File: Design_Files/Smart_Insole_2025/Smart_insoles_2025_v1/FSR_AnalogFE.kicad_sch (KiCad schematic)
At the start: 33 parts, among them J1 Conn_01x20, U8 MCP6004-I_ST, U9 MCP6004-I_ST

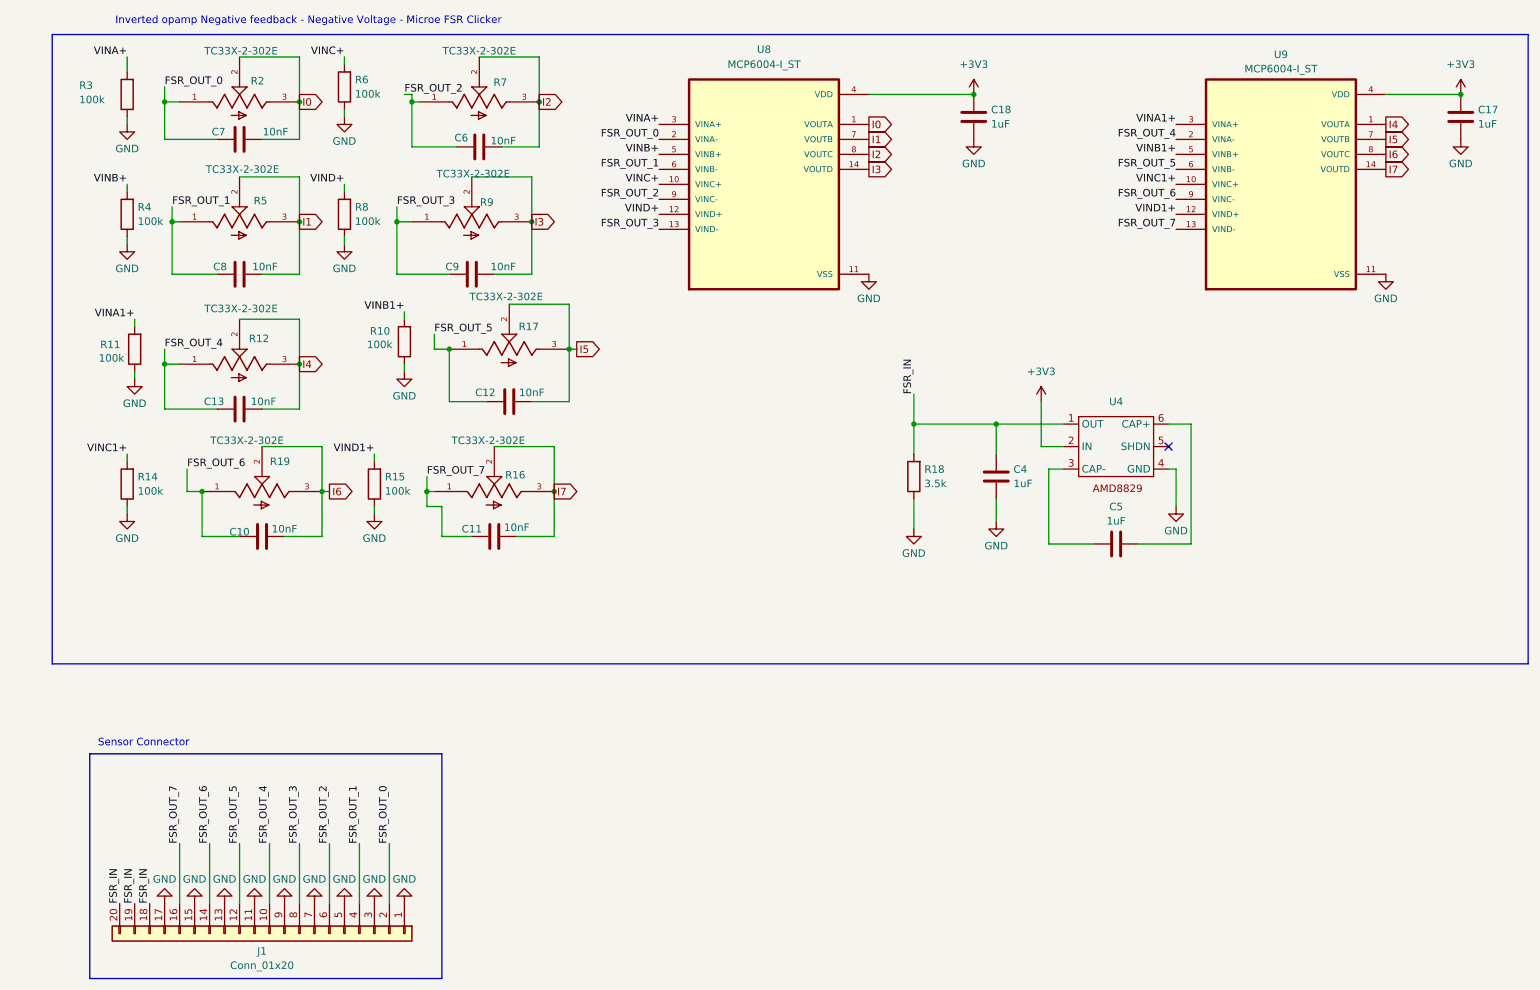
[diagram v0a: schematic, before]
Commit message: SCH: Added test points on idle MCU pins and Power supply. Added ON/OFF switch on VSEL.
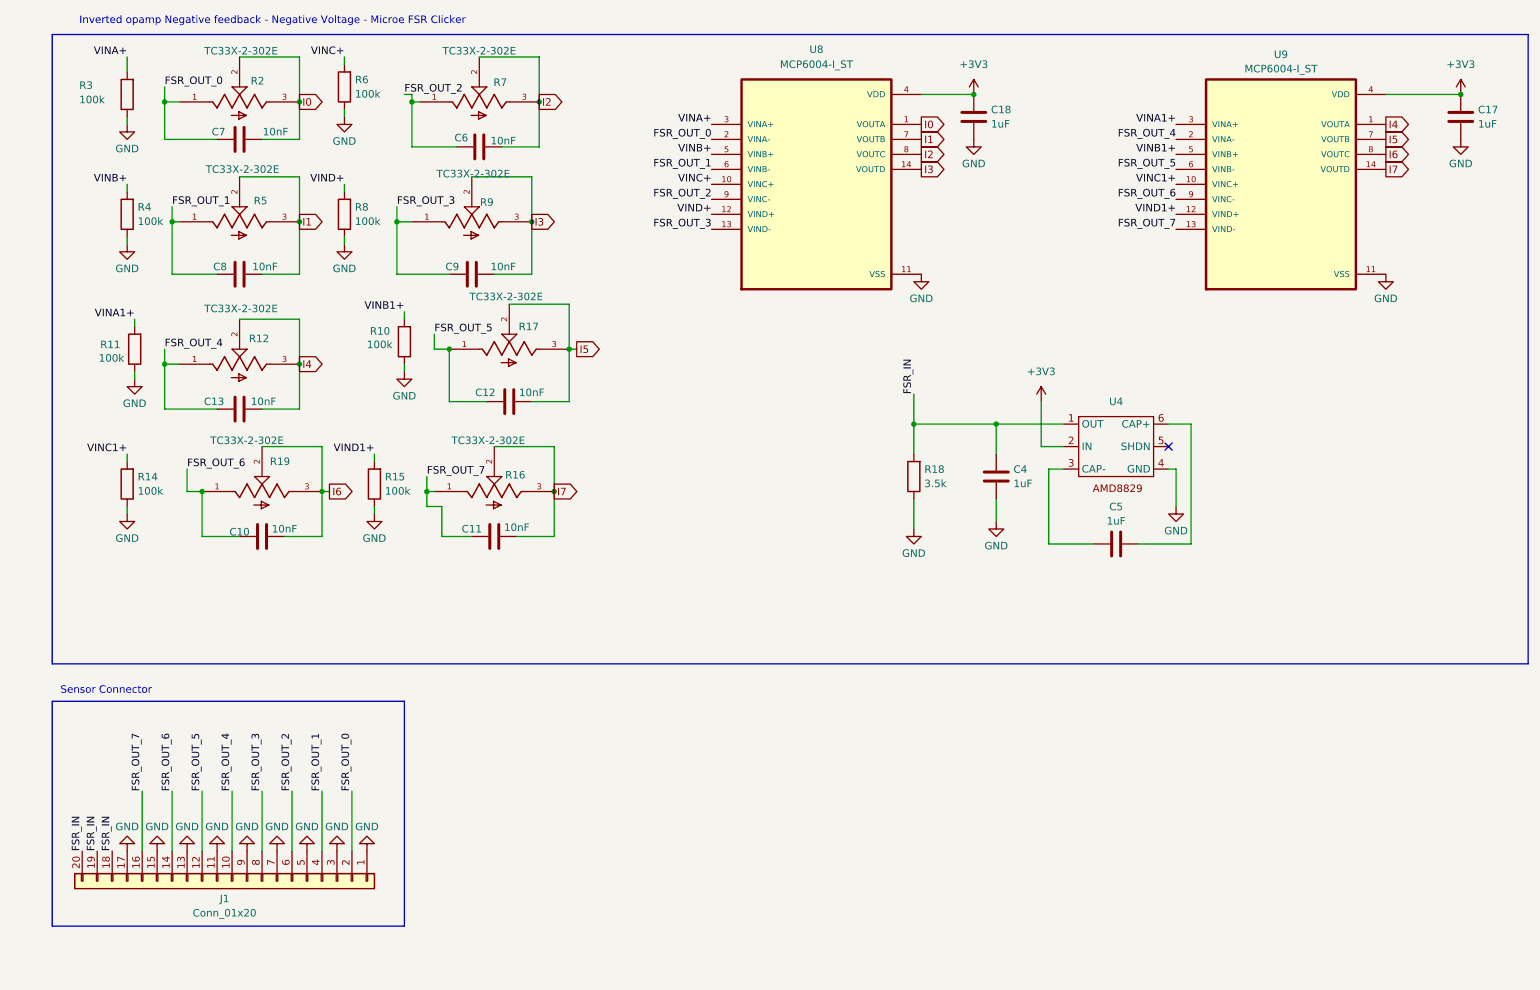
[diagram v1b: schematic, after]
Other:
- moved on the sheet: J1, U8

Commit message: PCB: Added 3d models to all components. Also preliminar routing of componentes. Component placemente needs checking.
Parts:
- C10, C11, C12, C13, C6, C7, C8, C9: footprint Capacitor_SMD:C_0805_2012Metric -> Capacitor_SMD:C_0805_2012Metric_Pad1.18x1.45mm_HandSolder
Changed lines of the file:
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@@
 			)
 		)
-		(property "Footprint" "Capacitor_SMD:C_0805_2012Metric"
+		(property "Footprint" "Capacitor_SMD:C_0805_2012Metric_Pad1.18x1.45mm_HandSolder"
 			(at 101.6 37.1348 0)
 			(effects
@@
 			)
 		)
-		(property "Footprint" "Capacitor_SMD:C_0805_2012Metric"
+		(property "Footprint" "Capacitor_SMD:C_0805_2012Metric_Pad1.18x1.45mm_HandSolder"
 			(at 106.68 80.3148 0)
 			(effects
@@
 			)
 		)
-		(property "Footprint" "Capacitor_SMD:C_0805_2012Metric"
+		(property "Footprint" "Capacitor_SMD:C_0805_2012Metric_Pad1.18x1.45mm_HandSolder"
 			(at 60.96 35.8648 0)
 			(effects
@@
 			)
 		)
-		(property "Footprint" "Capacitor_SMD:C_0805_2012Metric"
+		(property "Footprint" "Capacitor_SMD:C_0805_2012Metric_Pad1.18x1.45mm_HandSolder"
 			(at 104.14 103.1748 0)
 			(effects
@@
 			)
 		)
-		(property "Footprint" "Capacitor_SMD:C_0805_2012Metric"
+		(property "Footprint" "Capacitor_SMD:C_0805_2012Metric_Pad1.18x1.45mm_HandSolder"
 			(at 100.33 58.7248 0)
 			(effects
@@
 			)
 		)
-		(property "Footprint" "Capacitor_SMD:C_0805_2012Metric"
+		(property "Footprint" "Capacitor_SMD:C_0805_2012Metric_Pad1.18x1.45mm_HandSolder"
 			(at 60.96 58.7248 0)
 			(effects
@@
 			)
 		)
-		(property "Footprint" "Capacitor_SMD:C_0805_2012Metric"
+		(property "Footprint" "Capacitor_SMD:C_0805_2012Metric_Pad1.18x1.45mm_HandSolder"
 			(at 64.77 103.1748 0)
 			(effects
@@
 			)
 		)
+		(property "MPN" ""
+			(at 57.15 50.8 0)
+			(effects
+				(font
+					(size 1.27 1.27)
+				)
+				(hide yes)
+			)
+		)
+		(property "Manufacturer" ""
+			(at 57.15 50.8 0)
+			(effects
+				(font
+					(size 1.27 1.27)
+				)
+				(hide yes)
+			)
+		)
+		(property "3D Model" ""
+			(at 57.15 50.8 0)
+			(effects
+				(font
+					(size 1.27 1.27)
+				)
+				(hide yes)
+			)
+		)
+		(property "Notes" ""
+			(at 57.15 50.8 0)
+			(effects
+				(font
+					(size 1.27 1.27)
+				)
+				(hide yes)
+			)
+		)
+		(property "LCSC Part #" ""
+			(at 57.15 50.8 0)
+			(effects
+				(font
+					(size 1.27 1.27)
+				)
+				(hide yes)
+			)
+		)
+		(property "LCSC MPN" ""
+			(at 57.15 50.8 0)
+			(effects
+				(font
+					(size 1.27 1.27)
+				)
+				(hide yes)
+			)
+		)
+		(property "LCSC MANUFACTURER" ""
+			(at 57.15 50.8 0)
+			(effects
+				(font
+					(size 1.27 1.27)
+				)
+				(hide yes)
+			)
+		)
+		(property "Teste Fabricante" ""
+			(at 57.15 50.8 0)
+			(effects
+				(font
+					(size 1.27 1.27)
+				)
+				(hide yes)
+			)
+		)
+		(property "Teste Numero de parte" ""
+			(at 57.15 50.8 0)
+			(effects
+				(font
+					(size 1.27 1.27)
+				)
+				(hide yes)
+			)
+		)
 		(pin "3"
 		)
@@
 			)
 		)
-		(property "Footprint" "Capacitor_SMD:C_0805_2012Metric"
+		(property "Footprint" "Capacitor_SMD:C_0805_2012Metric_Pad1.18x1.45mm_HandSolder"
 			(at 60.96 81.5848 0)
 			(effects
@@
 				)
 				(justify bottom)
-				(hide yes)
 			)
 		)
@@
 				(hide yes)
 			)
+		)
+		(property "MPN" ""
+			(at 60.96 96.52 0)
+			(effects
+				(font
+					(size 1.27 1.27)
+				)
+				(hide yes)
+			)
+		)
+		(property "Manufacturer" ""
+			(at 60.96 96.52 0)
+			(effects
+				(font
+					(size 1.27 1.27)
+				)
+				(hide yes)
+			)
+		)
+		(property "3D Model" ""
+			(at 60.96 96.52 0)
+			(effects
+				(font
+					(size 1.27 1.27)
+				)
+				(hide yes)
+			)
+		)
+		(property "Notes" ""
+			(at 60.96 96.52 0)
+			(effects
+				(font
+					(size 1.27 1.27)
+				)
+				(hide yes)
+			)
+		)
+		(property "LCSC Part #" ""
+			(at 60.96 96.52 0)
+			(effects
+				(font
+					(size 1.27 1.27)
+				)
+				(hide yes)
+			)
+		)
+		(property "LCSC MPN" ""
+			(at 60.96 96.52 0)
+			(effects
+				(font
+					(size 1.27 1.27)
+				)
+				(hide yes)
+			)
+		)
+		(property "LCSC MANUFACTURER" ""
+			(at 60.96 96.52 0)
+			(effects
+				(font
+					(size 1.27 1.27)
+				)
+				(hide yes)
+			)
+		)
+		(property "Teste Fabricante" ""
+			(at 60.96 96.52 0)
+			(effects
+				(font
+					(size 1.27 1.27)
+				)
+				(hide yes)
+			)
+		)
+		(property "Teste Numero de parte" ""
+			(at 60.96 96.52 0)
+			(effects
+				(font
+					(size 1.27 1.27)
+				)
+				(hide yes)
+			)

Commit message: PCB:USB Differential pair Impedance calculation and Routing. Also Organized Silkscreen. Added text polarity to battery, boot and rst buttons, and RX TX
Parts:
- renumbered R2 to PT0, R5 to PT1, R7 to PT2, R9 to PT3, R12 to PT4, R17 to PT5, R19 to PT6, R16 to PT7
